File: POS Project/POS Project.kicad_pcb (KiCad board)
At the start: 2 copper layers, 59 parts, among them J1 JST_2mm_LiPo, J2 Conn_01x05_Socket, P1 USB_C_Plug_USB2.0, SW1 SW_Push, SW2 SW_Push, U1 SIM7600x, U2 MCP73831-2-OT, U4 SMF05C, U5 GSM_ANT, U6 GSM_ANT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

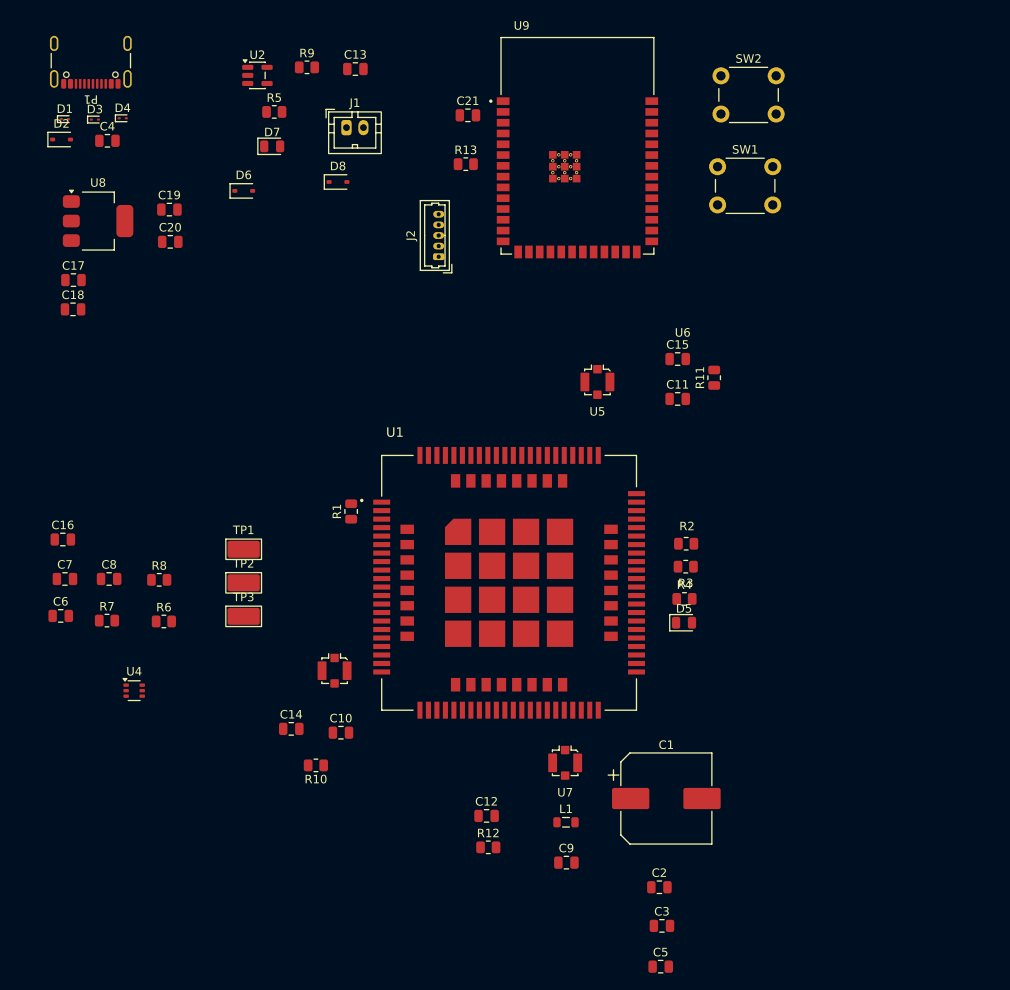
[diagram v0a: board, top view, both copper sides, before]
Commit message: organized PCB components
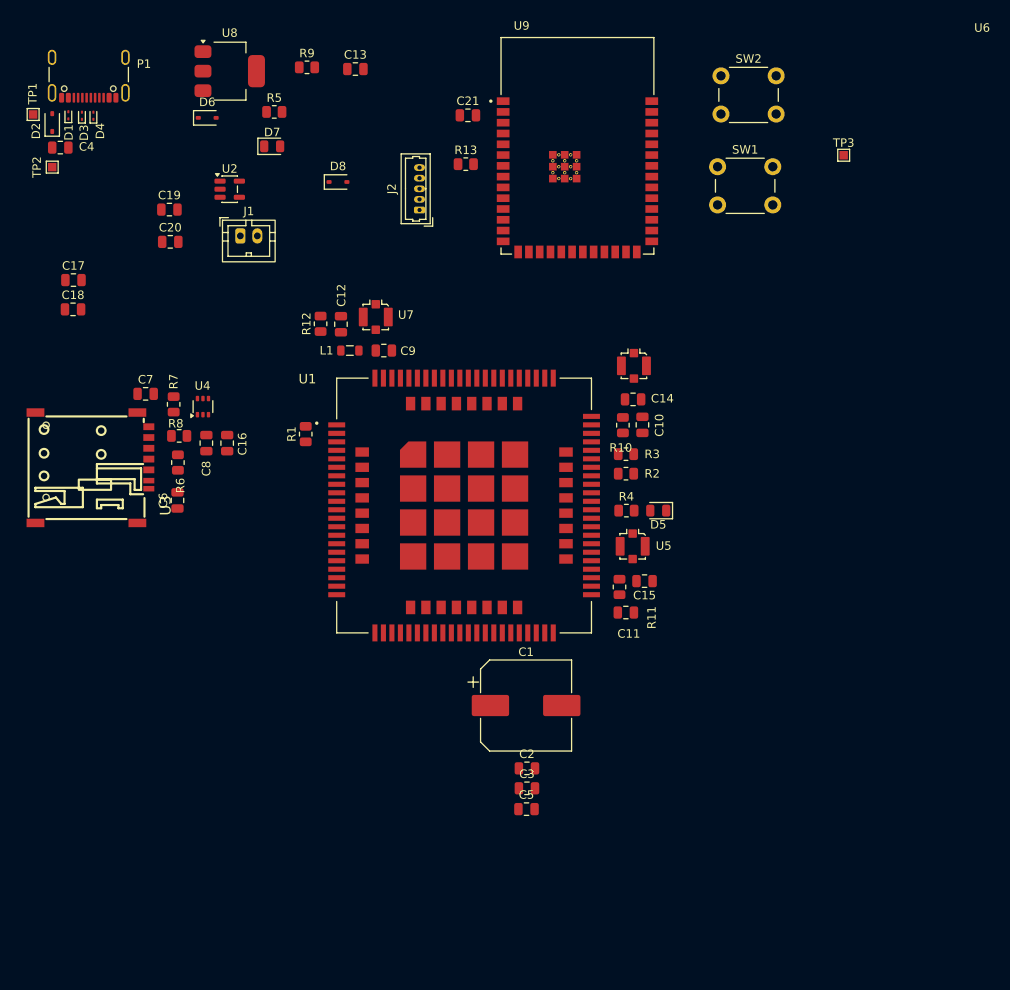
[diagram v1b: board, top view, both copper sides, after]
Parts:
- added U3: SMN-303, SMN-303:SIM-SMD_SMN-303, F.Cu at (20.8, 63.8)
- TP1, TP2, TP3: footprint TestPoint:TestPoint_Keystone_5019_Miniature -> TestPoint:TestPoint_Pad_1.0x1.0mm
- moved TP3 89.1 mm to (109.3, 26.9)
- moved R12 64.7 mm to (47.7, 46.8), turned to 90 degrees
- moved C9 64.0 mm to (55.1, 50.0)
- moved L1 61.1 mm to (51.1, 50.0), turned to 180 degrees
- moved C12 60.4 mm to (50.1, 46.9), turned to 90 degrees
- moved U7 57.0 mm to (54.2, 46.0)
- moved TP1 56.9 mm to (13.8, 22.1)
- moved C14 55.9 mm to (84.5, 55.7), turned to 180 degrees
- moved R10 54.0 mm to (83.3, 58.7), turned to 90 degrees
- moved TP2 53.9 mm to (16.1, 28.4), turned to 90 degrees
- moved C10 50.7 mm to (85.6, 58.7), turned to -90 degrees
- moved U6 50.3 mm to (84.6, 51.8)
- moved U4 34.4 mm to (33.9, 56.5), turned to 90 degrees
- moved R11 27.0 mm to (82.9, 77.8)
- moved R7 26.6 mm to (30.4, 56.3), turned to -90 degrees
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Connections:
- R12 pad 2: unconnected-(R12-Pad2) -> /VCC_3V3
- U4 pad 1: /CLK EN -> /DATA EN
- U4 pad 3: /RST EN -> /SIM1 VCC
- U4 pad 4: /DATA EN -> /RST EN
- U4 pad 6: /SIM1 VCC -> /CLK EN

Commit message: added PCB routs
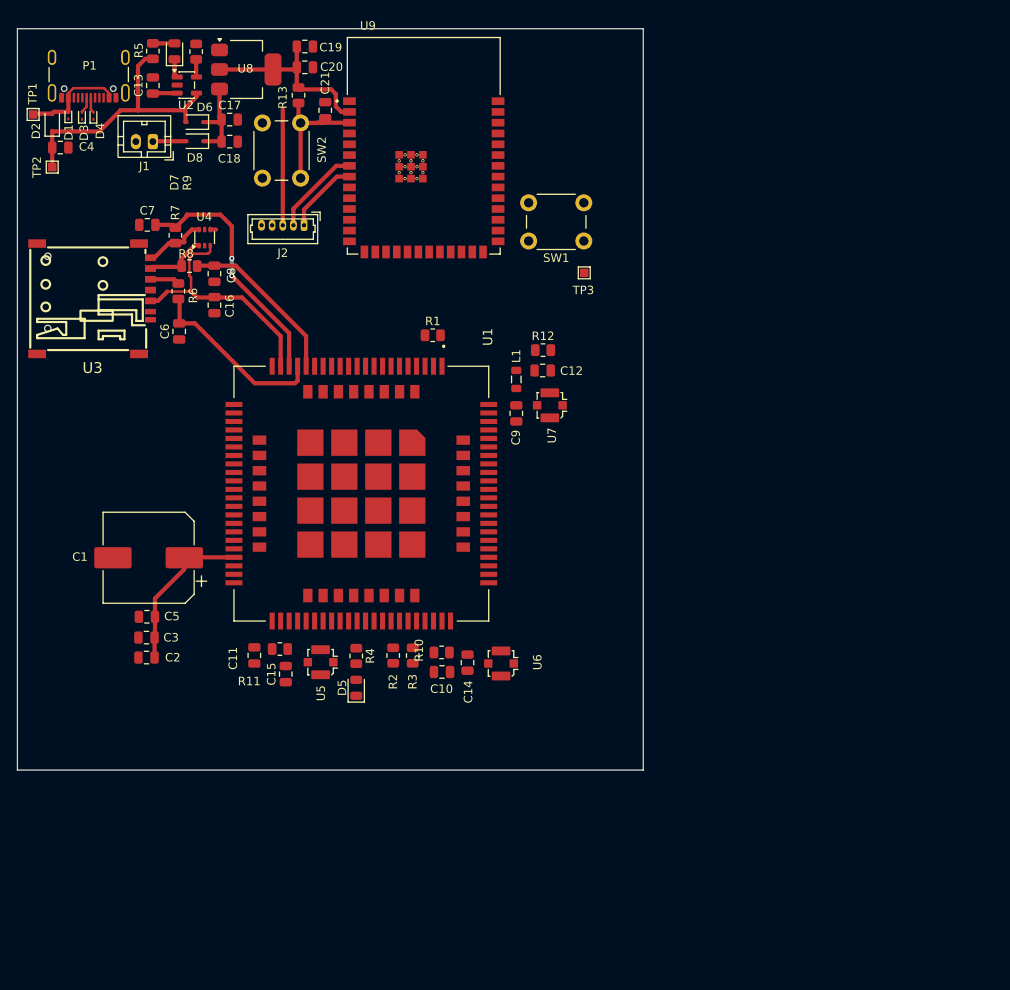
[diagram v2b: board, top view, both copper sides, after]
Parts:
- moved C5 50.1 mm to (27.2, 81.3), turned to 180 degrees
- moved SW2 49.8 mm to (45.4, 23.1), turned to -90 degrees
- moved C3 48.2 mm to (27.2, 83.8), turned to 180 degrees
- moved C1 47.7 mm to (27.4, 74.3), turned to 180 degrees
- moved C2 46.7 mm to (27.2, 86.1), turned to 180 degrees
- moved C11 44.0 mm to (39.9, 85.8), turned to 90 degrees
- moved C15 43.6 mm to (43.6, 88.0), turned to 90 degrees
- moved D5 41.2 mm to (51.9, 89.7), turned to 90 degrees
- moved R11 40.7 mm to (42.9, 85.1), turned to 0 degrees
- moved U5 39.2 mm to (47.7, 86.7), turned to -90 degrees
- moved U6 38.4 mm to (69.0, 86.8), turned to -90 degrees
- moved C10 37.5 mm to (62.0, 87.8), turned to 180 degrees
- moved C14 36.6 mm to (65.0, 86.7), turned to 90 degrees
- moved R4 36.1 mm to (51.9, 85.9), turned to -90 degrees
- moved R2 34.8 mm to (56.2, 85.9), turned to 90 degrees
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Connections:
- U9 pad 13: unconnected-(U9-IO19-Pad13) -> /GPIO19
- U9 pad 14: unconnected-(U9-IO20-Pad14) -> /GPIO20
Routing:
- net /VCC_3V3: track 0.00 -> 36.1 mm
- net VUSB: track 0.00 -> 32.1 mm
- net /SIM1 CLK: track 0.00 -> 29.7 mm, vias 0 -> 2
- net /SIM1 VCC: track 0.00 -> 28.3 mm
- net V_Batt: track 0.00 -> 25.9 mm
- net /SIM1 RST: track 0.00 -> 21.3 mm
- net /SIM1 DATA: track 0.00 -> 19.8 mm
- net Net-(U9-EN): track 0.00 -> 16.1 mm
- net Net-(D1-A2): track 0.00 -> 12.3 mm
- net VIN: track 0.00 -> 10.6 mm
- net /DATA: track 0.00 -> 10.6 mm
- net /STROBE: track 0.00 -> 8.81 mm
- net /DATA EN: track 0.00 -> 7.49 mm
- net /CLK EN: track 0.00 -> 7.45 mm
- net /RST EN: track 0.00 -> 4.18 mm
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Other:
- board outline added: 73.7 x 87.3 mm

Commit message: made final changes to pcb
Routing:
- net GND: track 0.00 -> 71.0 mm, vias 0 -> 136
- net V_Batt: track 25.9 -> 80.9 mm, vias 0 -> 4
- net /RXD: track 0.00 -> 53.5 mm, vias 0 -> 2
- net /TXD: track 0.00 -> 47.6 mm, vias 0 -> 2
- net 1V8: track 0.00 -> 47.5 mm, vias 0 -> 2
- net /VCC_3V3: track 36.1 -> 82.6 mm
- net /GPIO19: track 1.93 -> 44.3 mm, vias 0 -> 4
- net /GPIO20: track 1.82 -> 43.0 mm, vias 0 -> 4
- net /RESET: track 0.00 -> 29.8 mm, vias 0 -> 2
- net /ESP0/STAT: track 0.00 -> 13.9 mm
- net /RST EN: track 4.18 -> 13.5 mm, vias 0 -> 2
- net /AUX ANT: track 0.00 -> 6.02 mm
- net /Main ANT: track 0.00 -> 5.48 mm
- net Net-(C14-Pad2): track 0.00 -> 5.11 mm
- net Net-(C15-Pad2): track 0.00 -> 4.88 mm
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- added copper zone on B.Cu, net GND
- added copper zone on F.Cu, net GND
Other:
- board size 73.7 x 87.3 mm -> 71 x 82.8 mm

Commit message: created fabrication files
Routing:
- net GND: vias 136 -> 173
